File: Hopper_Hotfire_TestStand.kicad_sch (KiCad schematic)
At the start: 28 parts

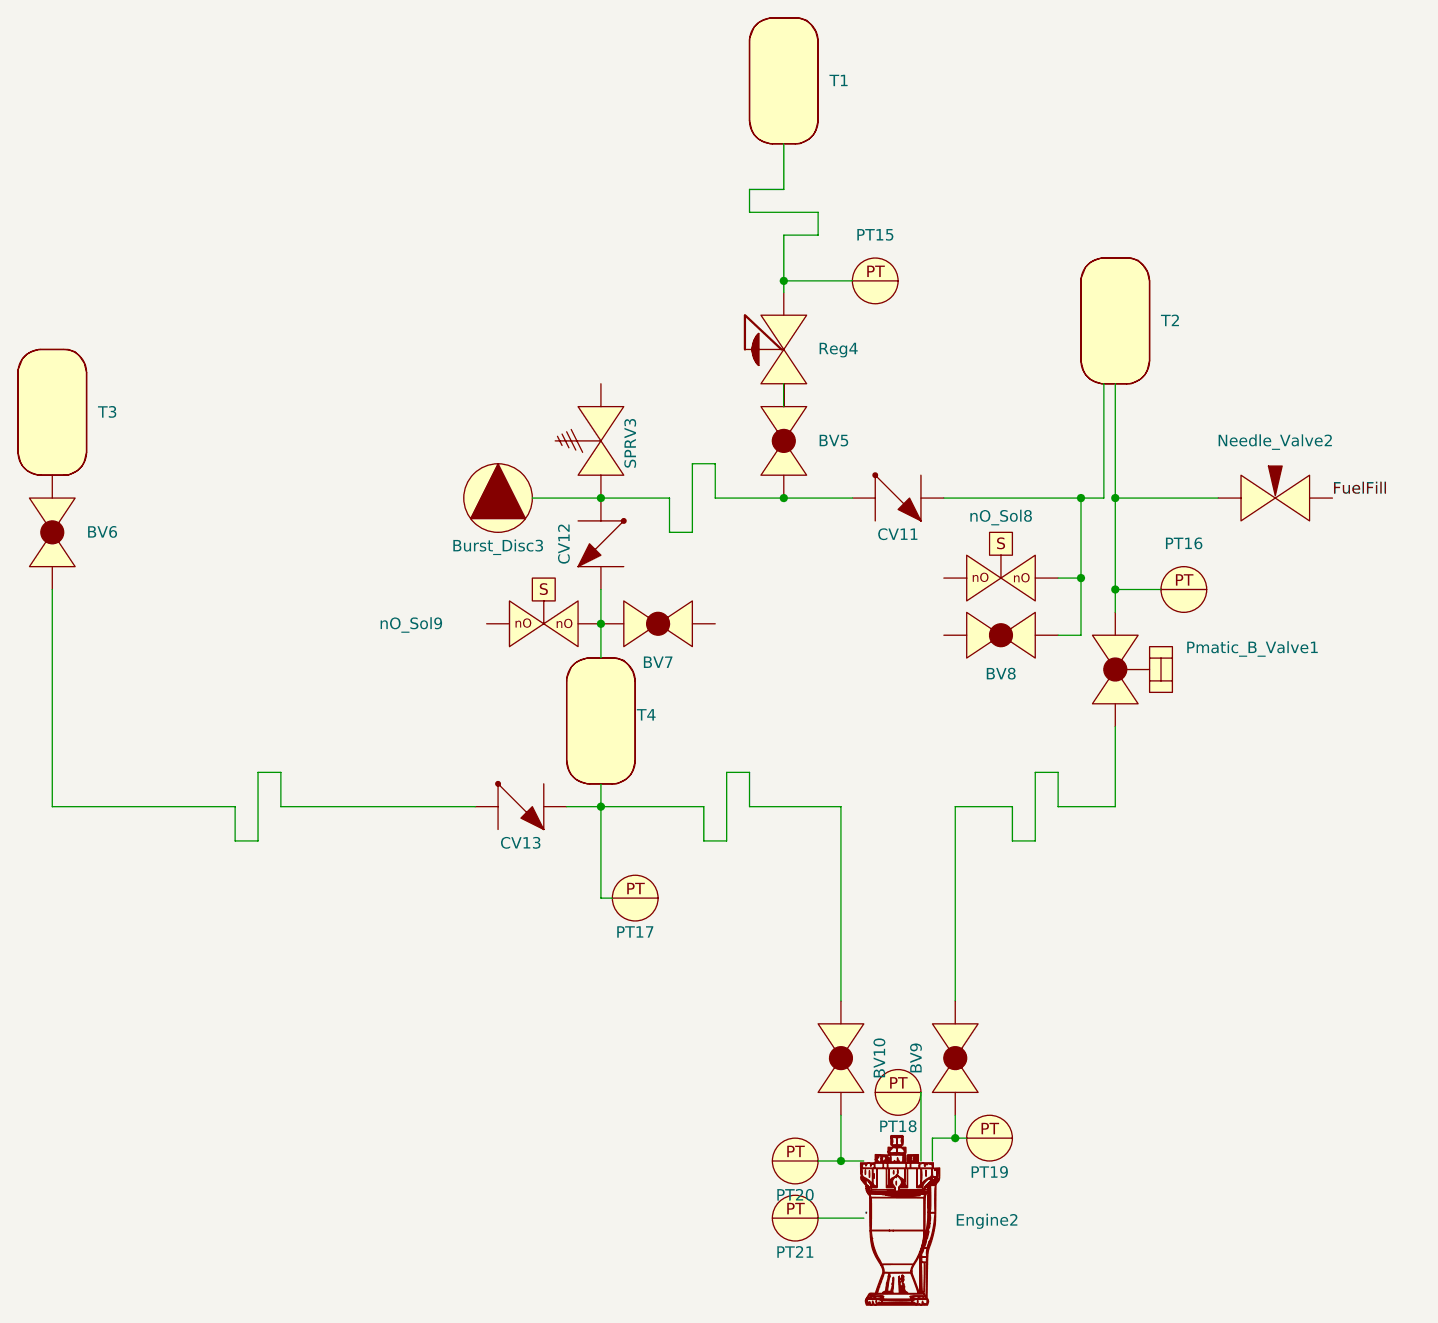
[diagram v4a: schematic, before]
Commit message: Added Igniter + Hopper Engine test
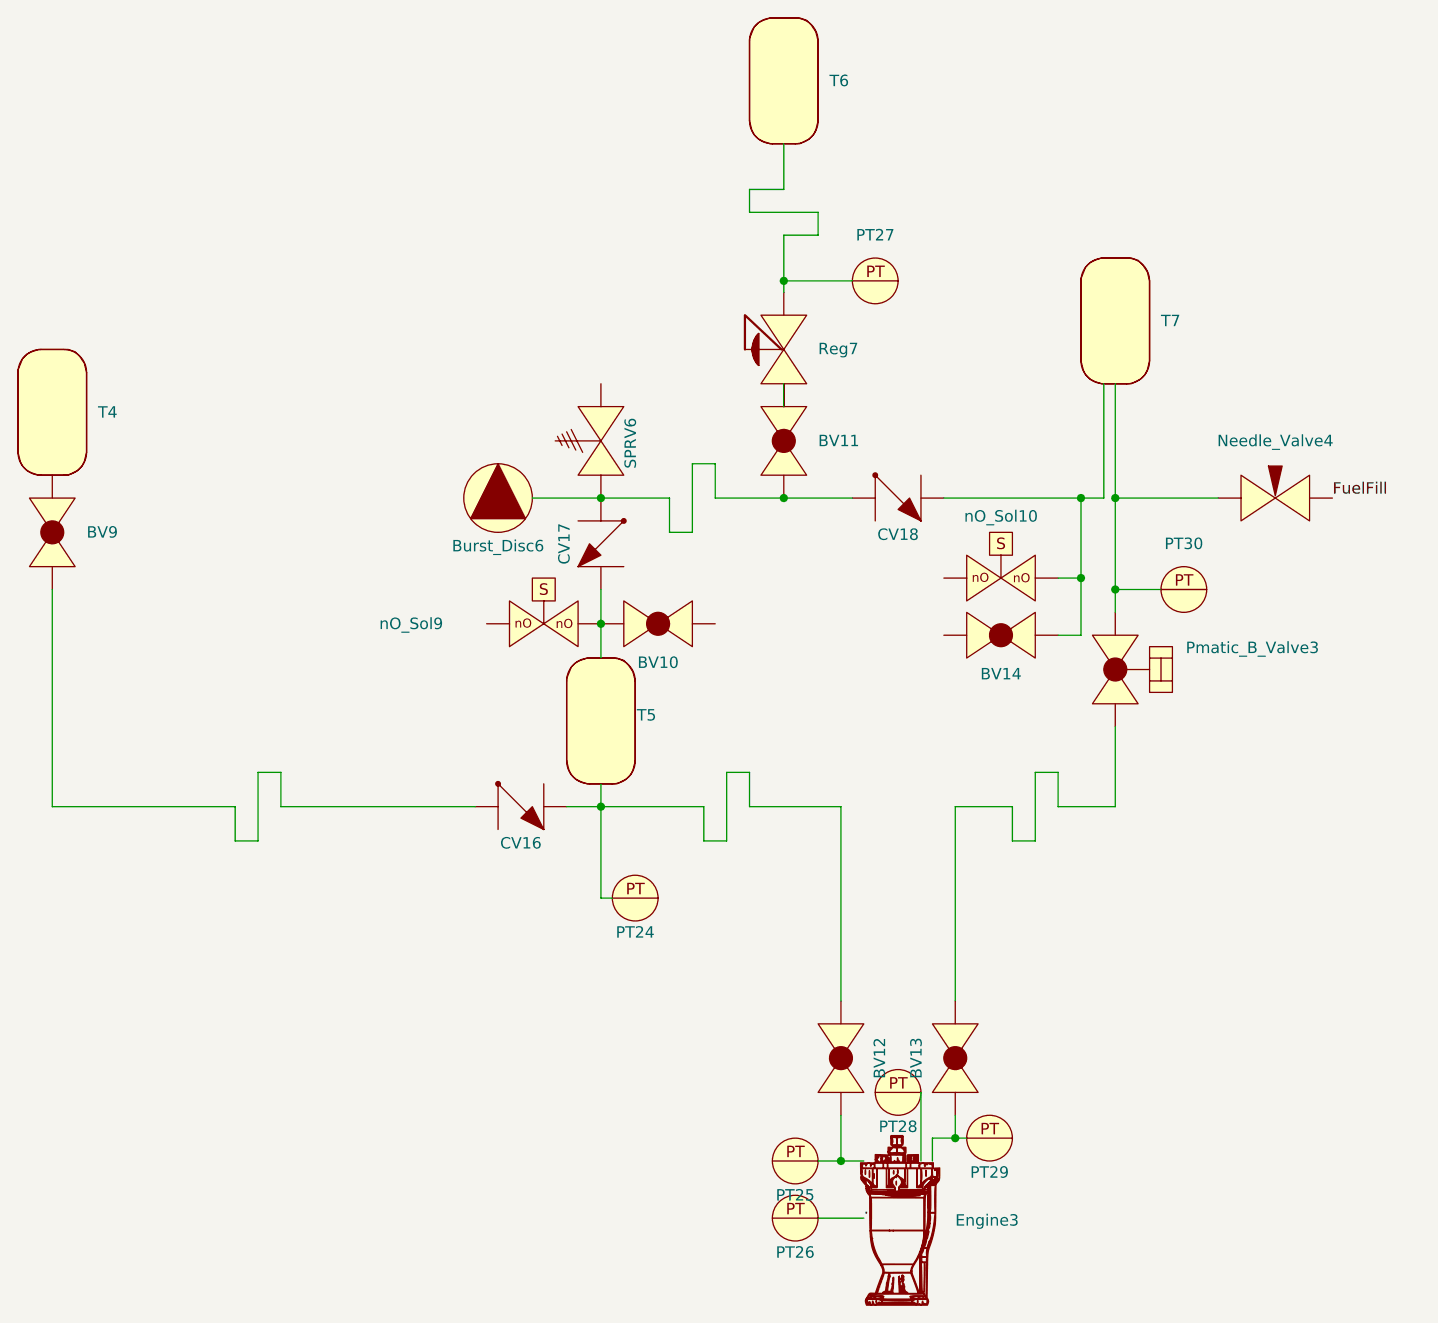
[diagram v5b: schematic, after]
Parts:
- renumbered BV7 to BV10, BV5 to BV11, BV10 to BV12, BV9 to BV13, BV8 to BV14, BV6 to BV9, Burst_Disc3 to Burst_Disc6, CV13 to CV16, CV12 to CV17, CV11 to CV18, Engine2 to Engine3, Needle_Valve2 to Needle_Valve4, PT17 to PT24, PT20 to PT25, PT21 to PT26, PT15 to PT27, PT18 to PT28, PT19 to PT29, PT16 to PT30, Pmatic_B_Valve1 to Pmatic_B_Valve3, Reg4 to Reg7, SPRV3 to SPRV6, T3 to T4, T4 to T5, T1 to T6, T2 to T7, nO_Sol8 to nO_Sol10
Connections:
- net at CV16.: now also BV12., PT24., T5.; no longer BV9.
- net at BV14.: now also CV18., nO_Sol10.
- net at PT29.: now also BV13., Engine3.
- net at Pmatic_B_Valve3.: now also BV13.
- net at PT27.: now also Reg7., T6.
- new net: BV9., CV16.
- new net: BV12., Engine3., PT25.
- new net: BV11., Burst_Disc6., CV17., CV18., SPRV6.
- new net: Needle_Valve4., PT30., Pmatic_B_Valve3., T7.
- now unconnected: Burst_Disc6., Engine3., Engine3., PT24., PT25., PT30., SPRV6., T6., T7., nO_Sol10.
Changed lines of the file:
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@@
 	(label "."
 		(at 139.7 149.86 0)
-		(fields_autoplaced yes)
 		(effects
 			(font
@@
 	(label "FuelFill"
 		(at 191.77 69.85 0)
-		(fields_autoplaced yes)
 		(effects
 			(font
@@
 		(on_board yes)
 		(dnp no)
-		(property "Reference" "PT18"
+		(property "Reference" "PT28"
 			(at 143.51 139.7 0)
 			(effects
@@
 			(project "P_IDs"
 				(path "/045f1f05-3134-4b6d-91b6-463031104f1e/12264f82-10ad-4f8b-aee0-7883d457c15c"
-					(reference "PT18")
+					(reference "PT28")
 					(unit 1)
 				)
@@
 		(on_board yes)
 		(dnp no)
-		(property "Reference" "CV13"
+		(property "Reference" "CV16"
 			(at 101.6 108.204 0)
 			(effects
@@
 			(project "P_IDs"
 				(path "/045f1f05-3134-4b6d-91b6-463031104f1e/12264f82-10ad-4f8b-aee0-7883d457c15c"
-					(reference "CV13")
+					(reference "CV16")
 					(unit 1)
 				)
@@
 		(dnp no)
 		(fields_autoplaced yes)
-		(property "Reference" "BV6"
+		(property "Reference" "BV9"
 			(at 53.34 73.6599 90)
 			(effects
@@
 			(project "P_IDs"
 				(path "/045f1f05-3134-4b6d-91b6-463031104f1e/12264f82-10ad-4f8b-aee0-7883d457c15c"
-					(reference "BV6")
+					(reference "BV9")
 					(unit 1)
 				)
@@
 		(on_board yes)
 		(dnp no)
-		(property "Reference" "BV8"
+		(property "Reference" "BV14"
 			(at 154.94 89.408 0)
 			(effects
@@
 			(project "P_IDs"
 				(path "/045f1f05-3134-4b6d-91b6-463031104f1e/12264f82-10ad-4f8b-aee0-7883d457c15c"
-					(reference "BV8")
+					(reference "BV14")
 					(unit 1)
 				)
@@
 		(on_board yes)
 		(dnp no)
-		(property "Reference" "BV10"
+		(property "Reference" "BV12"
 			(at 141.478 132.08 0)
 			(effects
@@
 			(project "P_IDs"
 				(path "/045f1f05-3134-4b6d-91b6-463031104f1e/12264f82-10ad-4f8b-aee0-7883d457c15c"
-					(reference "BV10")
+					(reference "BV12")
 					(unit 1)
 				)
@@
 		(on_board yes)
 		(dnp no)
-		(property "Reference" "PT19"
+		(property "Reference" "PT29"
 			(at 153.67 144.78 0)
 			(effects
@@
 			(project "P_IDs"
 				(path "/045f1f05-3134-4b6d-91b6-463031104f1e/12264f82-10ad-4f8b-aee0-7883d457c15c"
-					(reference "PT19")
+					(reference "PT29")
 					(unit 1)
 				)
@@
 		(dnp no)
 		(fields_autoplaced yes)
-		(property "Reference" "Engine2"
+		(property "Reference" "Engine3"
 			(at 149.86 150.1068 0)
 			(effects
@@
 			(project "P_IDs"
 				(path "/045f1f05-3134-4b6d-91b6-463031104f1e/12264f82-10ad-4f8b-aee0-7883d457c15c"
-					(reference "Engine2")
+					(reference "Engine3")
 					(unit 1)
 				)
@@
 		(on_board yes)
 		(dnp no)
-		(property "Reference" "CV11"
+		(property "Reference" "CV18"
 			(at 143.51 73.914 0)
 			(effects
@@
 			(project "P_IDs"
 				(path "/045f1f05-3134-4b6d-91b6-463031104f1e/12264f82-10ad-4f8b-aee0-7883d457c15c"
-					(reference "CV11")
+					(reference "CV18")
 					(unit 1)
 				)
@@
 		(on_board yes)
 		(dnp no)
-		(property "Reference" "PT21"
+		(property "Reference" "PT26"
 			(at 132.08 153.67 0)
 			(effects
@@
 			(project "P_IDs"
 				(path "/045f1f05-3134-4b6d-91b6-463031104f1e/12264f82-10ad-4f8b-aee0-7883d457c15c"
-					(reference "PT21")
+					(reference "PT26")
 					(unit 1)
 				)
@@
 		(on_board yes)
 		(dnp no)
-		(property "Reference" "nO_Sol8"
+		(property "Reference" "nO_Sol10"
 			(at 154.94 71.882 0)
 			(effects
@@
 			(project "P_IDs"
 				(path "/045f1f05-3134-4b6d-91b6-463031104f1e/12264f82-10ad-4f8b-aee0-7883d457c15c"
-					(reference "nO_Sol8")
+					(reference "nO_Sol10")
 					(unit 1)
 				)
@@
 		(on_board yes)
 		(dnp no)
-		(property "Reference" "Burst_Disc3"
+		(property "Reference" "Burst_Disc6"
 			(at 99.06 75.184 0)
 			(effects
@@
 			(project "P_IDs"
 				(path "/045f1f05-3134-4b6d-91b6-463031104f1e/12264f82-10ad-4f8b-aee0-7883d457c15c"
-					(reference "Burst_Disc3")
+					(reference "Burst_Disc6")
 					(unit 1)
 				)
@@
 		(on_board yes)
 		(dnp no)
-		(property "Reference" "PT17"
+		(property "Reference" "PT24"
 			(at 114.3 118.11 0)
 			(effects
@@
 			(project "P_IDs"
 				(path "/045f1f05-3134-4b6d-91b6-463031104f1e/12264f82-10ad-4f8b-aee0-7883d457c15c"
-					(reference "PT17")
+					(reference "PT24")
 					(unit 1)
 				)
@@
 		(dnp no)
 		(fields_autoplaced yes)
-		(property "Reference" "Needle_Valve2"
+		(property "Reference" "Needle_Valve4"
 			(at 185.42 63.5 0)
 			(effects
@@
 			(project "P_IDs"
 				(path "/045f1f05-3134-4b6d-91b6-463031104f1e/12264f82-10ad-4f8b-aee0-7883d457c15c"
-					(reference "Needle_Valve2")
+					(reference "Needle_Valve4")
 					(unit 1)
 				)
@@
 		(on_board yes)
 		(dnp no)
-		(property "Reference" "PT20"
+		(property "Reference" "PT25"
 			(at 132.08 147.32 0)
 			(effects
@@
 			(project "P_IDs"
 				(path "/045f1f05-3134-4b6d-91b6-463031104f1e/12264f82-10ad-4f8b-aee0-7883d457c15c"
-					(reference "PT20")
+					(reference "PT25")
 					(unit 1)
 				)
@@
 		(on_board yes)
 		(dnp no)
-		(property "Reference" "T4"
+		(property "Reference" "T5"
 			(at 115.57 93.98 0)
 			(effects
@@
 			(project "P_IDs"
 				(path "/045f1f05-3134-4b6d-91b6-463031104f1e/12264f82-10ad-4f8b-aee0-7883d457c15c"
-					(reference "T4")
+					(reference "T5")
 					(unit 1)
 				)
@@
 		(on_board yes)
 		(dnp no)
-		(property "Reference" "SPRV3"
+		(property "Reference" "SPRV6"
 			(at 113.792 63.754 0)
 			(effects
@@
 			(project "P_IDs"
 				(path "/045f1f05-3134-4b6d-91b6-463031104f1e/12264f82-10ad-4f8b-aee0-7883d457c15c"
-					(reference "SPRV3")
+					(reference "SPRV6")
 					(unit 1)
 				)
@@
 		(dnp no)
 		(fields_autoplaced yes)
-		(property "Reference" "BV5"
+		(property "Reference" "BV11"
 			(at 134.62 63.4999 90)
 			(effects
@@
 			(project "P_IDs"
 				(path "/045f1f05-3134-4b6d-91b6-463031104f1e/12264f82-10ad-4f8b-aee0-7883d457c15c"
-					(reference "BV5")
+					(reference "BV11")
 					(unit 1)
 				)
@@
 		(dnp no)
 		(fields_autoplaced yes)
-		(property "Reference" "Pmatic_B_Valve1"
+		(property "Reference" "Pmatic_B_Valve3"
 			(at 182.88 86.4868 90)
 			(effects
@@
 			(project ""
 				(path "/045f1f05-3134-4b6d-91b6-463031104f1e/12264f82-10ad-4f8b-aee0-7883d457c15c"
-					(reference "Pmatic_B_Valve1")
+					(reference "Pmatic_B_Valve3")
 					(unit 1)
 				)
@@
 		(dnp no)
 		(fields_autoplaced yes)
-		(property "Reference" "PT16"
+		(property "Reference" "PT30"
 			(at 175.26 74.93 0)
 			(effects
@@
 			(project "P_IDs"
 				(path "/045f1f05-3134-4b6d-91b6-463031104f1e/12264f82-10ad-4f8b-aee0-7883d457c15c"
-					(reference "PT16")
+					(reference "PT30")
 					(unit 1)
 				)
@@
 		(dnp no)
 		(fields_autoplaced yes)
-		(property "Reference" "PT15"
+		(property "Reference" "PT27"
 			(at 140.97 40.64 0)
 			(effects
@@
 			(project "P_IDs"
 				(path "/045f1f05-3134-4b6d-91b6-463031104f1e/12264f82-10ad-4f8b-aee0-7883d457c15c"
-					(reference "PT15")
+					(reference "PT27")
 					(unit 1)
 				)
@@
 		(dnp no)
 		(fields_autoplaced yes)
-		(property "Reference" "Reg4"
+		(property "Reference" "Reg7"
 			(at 134.62 53.2774 90)
 			(effects
@@
 			(project "P_IDs"
 				(path "/045f1f05-3134-4b6d-91b6-463031104f1e/12264f82-10ad-4f8b-aee0-7883d457c15c"
-					(reference "Reg4")
+					(reference "Reg7")
 					(unit 1)
 				)
@@
 		(dnp no)
 		(fields_autoplaced yes)
-		(property "Reference" "T1"
+		(property "Reference" "T6"
 			(at 135.89 23.4949 0)
 			(effects
@@
 			(project "P_IDs"
 				(path "/045f1f05-3134-4b6d-91b6-463031104f1e/12264f82-10ad-4f8b-aee0-7883d457c15c"
-					(reference "T1")
+					(reference "T6")
 					(unit 1)
 				)
@@
 		(on_board yes)
 		(dnp no)
-		(property "Reference" "BV7"
+		(property "Reference" "BV10"
 			(at 116.84 88.138 0)
 			(effects
@@
 			(project "P_IDs"
 				(path "/045f1f05-3134-4b6d-91b6-463031104f1e/12264f82-10ad-4f8b-aee0-7883d457c15c"
-					(reference "BV7")
+					(reference "BV10")
 					(unit 1)
 				)
@@
 		(on_board yes)
 		(dnp no)
-		(property "Reference" "CV12"
+		(property "Reference" "CV17"
 			(at 106.426 74.93 0)
 			(effects
@@
 			(project "P_IDs"
 				(path "/045f1f05-3134-4b6d-91b6-463031104f1e/12264f82-10ad-4f8b-aee0-7883d457c15c"
-					(reference "CV12")
+					(reference "CV17")
 					(unit 1)
 				)
@@
 		(dnp no)
 		(fields_autoplaced yes)
-		(property "Reference" "T3"
+		(property "Reference" "T4"
 			(at 54.61 60.3249 0)
 			(effects
@@
 			(project "P_IDs"
 				(path "/045f1f05-3134-4b6d-91b6-463031104f1e/12264f82-10ad-4f8b-aee0-7883d457c15c"
-					(reference "T3")
+					(reference "T4")
 					(unit 1)
 				)
@@
 		(dnp no)
 		(fields_autoplaced yes)
-		(property "Reference" "T2"
+		(property "Reference" "T7"
 			(at 172.72 50.1649 0)
 			(effects
@@
 			(project "P_IDs"
 				(path "/045f1f05-3134-4b6d-91b6-463031104f1e/12264f82-10ad-4f8b-aee0-7883d457c15c"
-					(reference "T2")
+					(reference "T7")
 					(unit 1)
 				)
@@
 		(on_board yes)
 		(dnp no)
-		(property "Reference" "BV9"
+		(property "Reference" "BV13"
 			(at 145.542 132.08 0)
 			(effects
@@
 			(project "P_IDs"
 				(path "/045f1f05-3134-4b6d-91b6-463031104f1e/12264f82-10ad-4f8b-aee0-7883d457c15c"
-					(reference "BV9")
-					(unit 1)
-				)
+					(reference "BV13")
+					(unit 1)
+				)

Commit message: overwrite
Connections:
- net at CV16.: now also BV12., PT24., T5.; no longer BV9.
- net at BV14.: now also CV18., nO_Sol10.
- net at PT29.: now also BV13., Engine3.
- net at Pmatic_B_Valve3.: now also BV13.
- net at PT27.: now also Reg7., T6.
- new net: BV9., CV16.
- new net: BV12., Engine3., PT25.
- new net: BV11., Burst_Disc6., CV17., CV18., SPRV6.
- new net: Needle_Valve4., PT30., Pmatic_B_Valve3., T7.
- now unconnected: Burst_Disc6., Engine3., Engine3., PT24., PT25., PT30., SPRV6., T6., T7., nO_Sol10.
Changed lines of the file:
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@@
 	(label "."
 		(at 139.7 149.86 0)
+		(fields_autoplaced yes)
 		(effects
 			(font
@@
 	(label "FuelFill"
 		(at 191.77 69.85 0)
+		(fields_autoplaced yes)
 		(effects
 			(font

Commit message: no message
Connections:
- net at CV16.: now also BV12., PT24., T5.; no longer BV9.
- net at BV14.: now also CV18., nO_Sol10.
- net at PT29.: now also BV13., Engine3.
- net at Pmatic_B_Valve3.: now also BV13.
- net at PT27.: now also Reg7., T6.
- new net: BV9., CV16.
- new net: BV12., Engine3., PT25.
- new net: BV11., Burst_Disc6., CV17., CV18., SPRV6.
- new net: Needle_Valve4., PT30., Pmatic_B_Valve3., T7.
- now unconnected: Burst_Disc6., Engine3., Engine3., PT24., PT25., PT30., SPRV6., T6., T7., nO_Sol10.
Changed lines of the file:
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@@
 	)
 	(symbol
+		(lib_name "PID_symbols:Check_Valve")
 		(lib_id "PID_symbols:Check_Valve")
 		(at 110.49 72.39 270)

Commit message: update
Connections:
- net at CV16.: now also BV12., PT24., T5.; no longer BV9.
- net at BV14.: now also CV18., nO_Sol10.
- net at PT29.: now also BV13., Engine3.
- net at Pmatic_B_Valve3.: now also BV13.
- net at PT27.: now also Reg7., T6.
- new net: BV9., CV16.
- new net: BV12., Engine3., PT25.
- new net: BV11., Burst_Disc6., CV17., CV18., SPRV6.
- new net: Needle_Valve4., PT30., Pmatic_B_Valve3., T7.
- now unconnected: Burst_Disc6., Engine3., Engine3., PT24., PT25., PT30., SPRV6., T6., T7., nO_Sol10.
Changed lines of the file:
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@@
 	)
 	(symbol
-		(lib_name "PID_symbols:Check_Valve")
 		(lib_id "PID_symbols:Check_Valve")
 		(at 110.49 72.39 270)
